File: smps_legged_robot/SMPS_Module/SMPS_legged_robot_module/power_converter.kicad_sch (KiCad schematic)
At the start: 101 parts, among them IC701 LTC3889EUKG#PBF, Q701 IPG20N06S4L26AATMA1, Q702 IPG20N06S4L26AATMA1, Q703 PMBT3906,215, Q704 PMBT3906,215, Q705 IPG20N06S4L26AATMA1, Q706 IPG20N06S4L26AATMA1, Q707 NMOS, Q708 NMOS

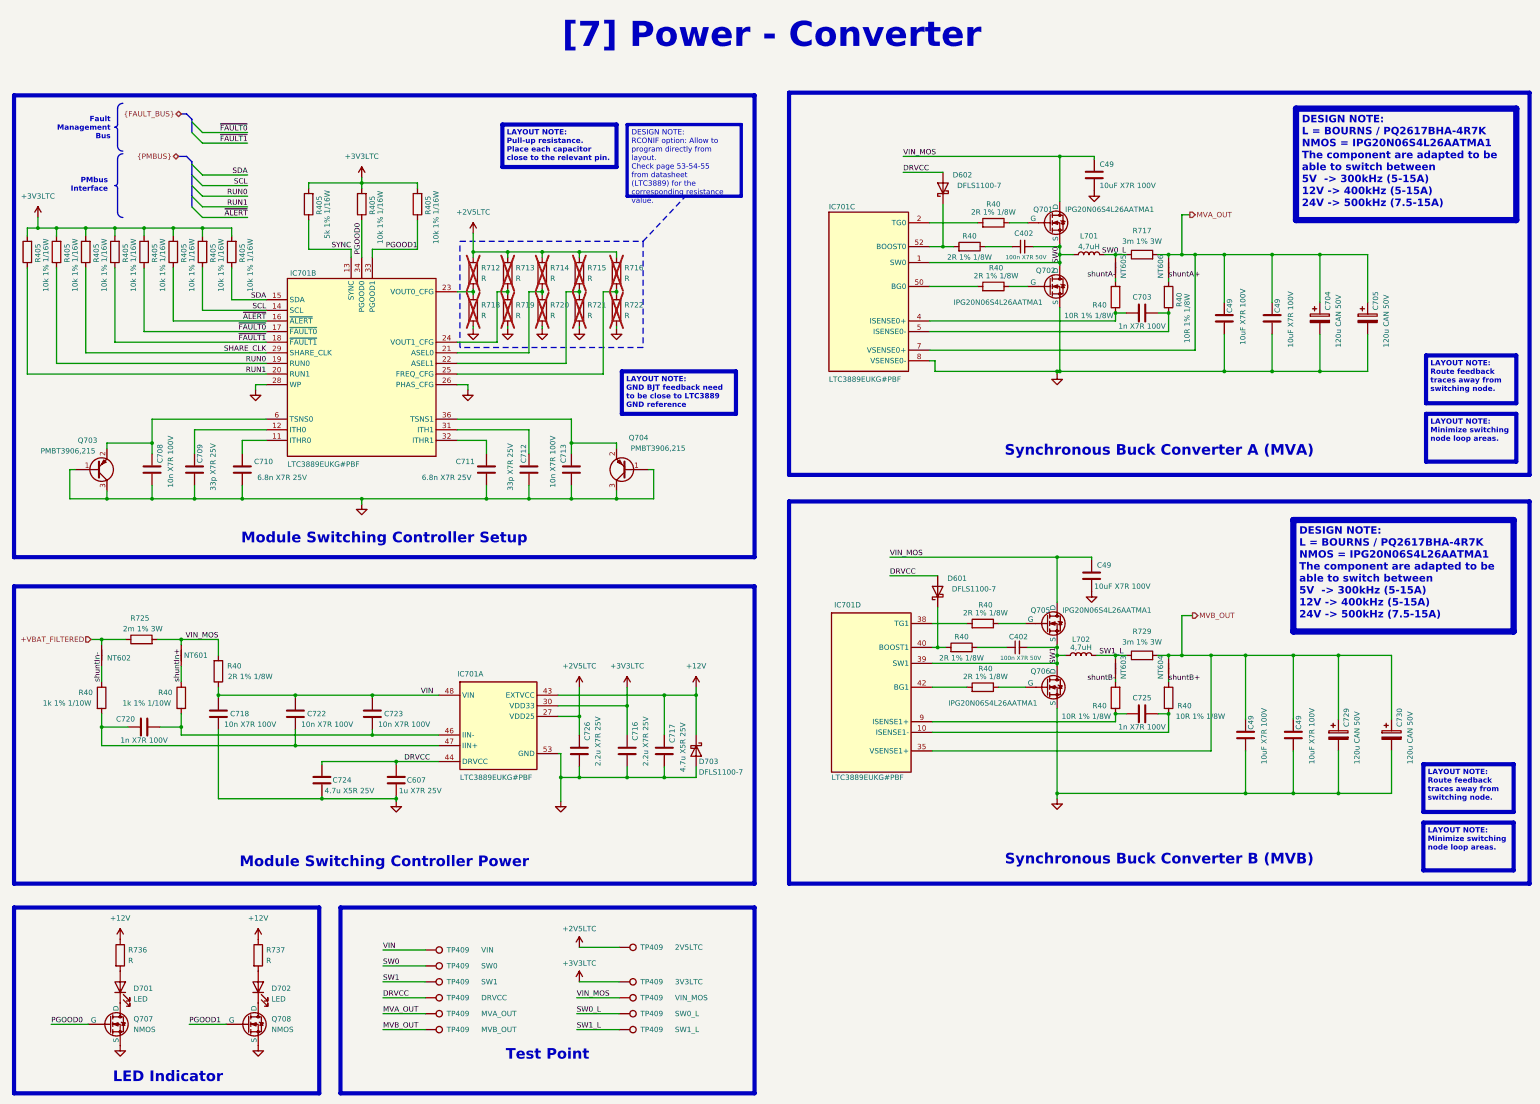
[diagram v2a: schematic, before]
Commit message: Rev 1.0 of smps finished -> waiting for verification
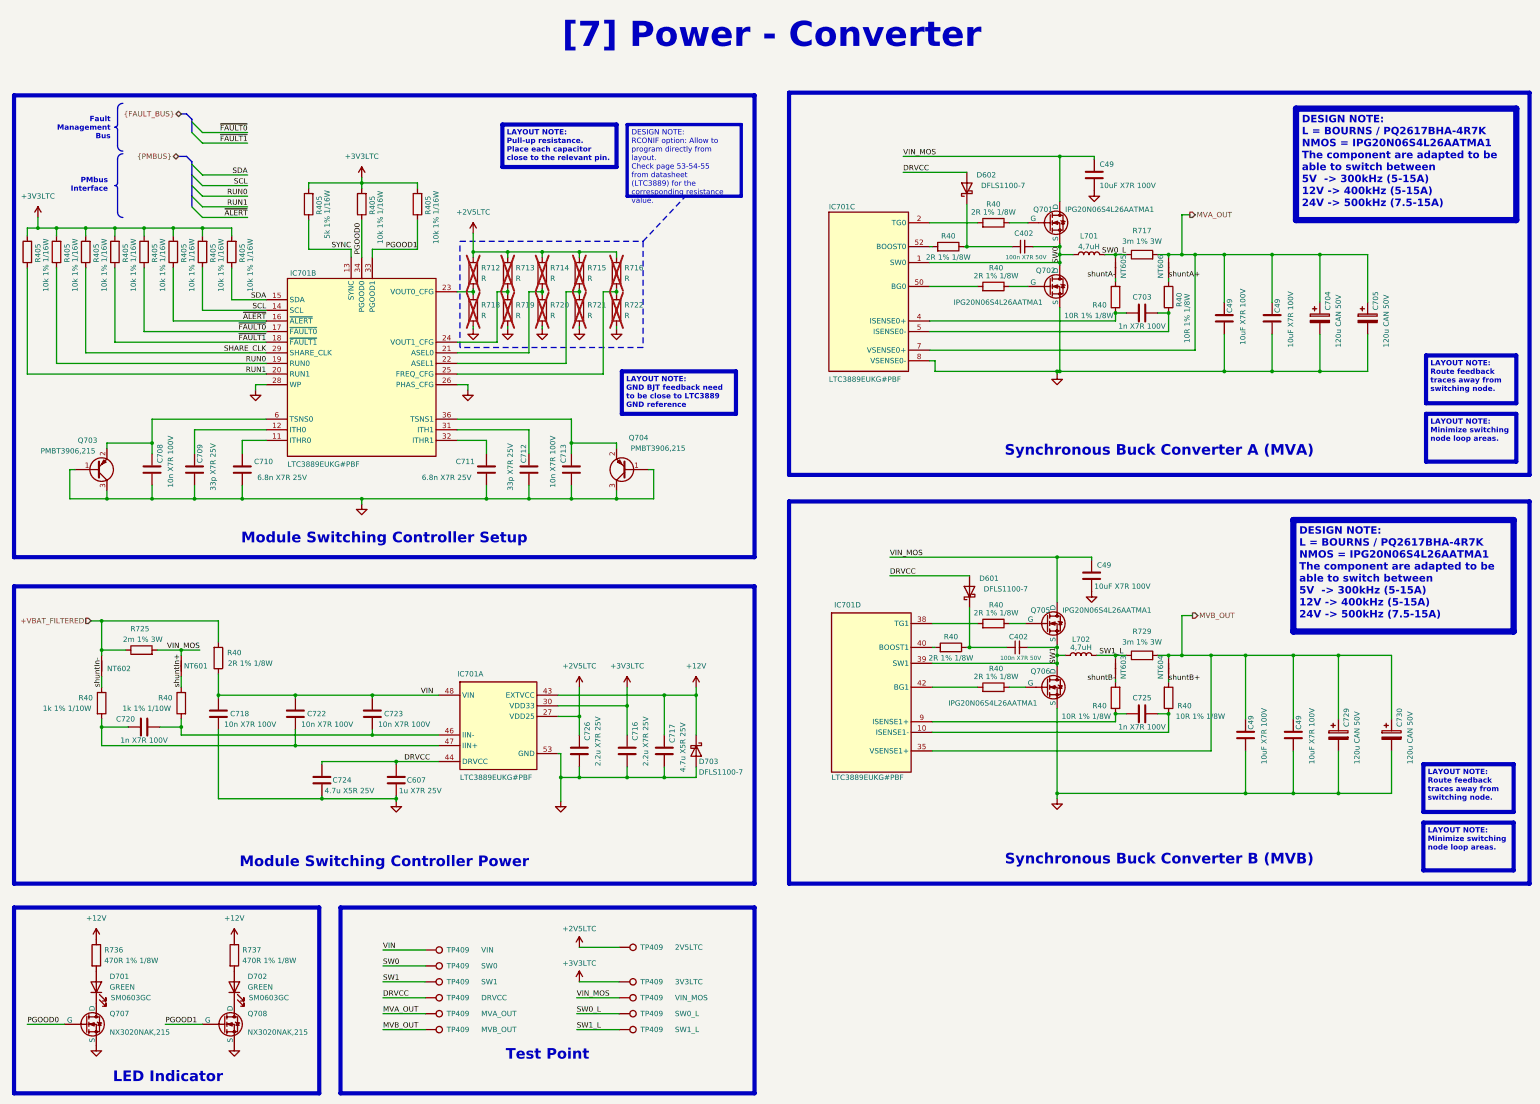
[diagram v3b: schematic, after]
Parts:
- D701, D702: value LED -> GREEN; footprint (none) -> LED_SMD:LED_0603_1608Metric; Digikey ref (none) -> 492-1324-1-ND; Manufacturer ref (none) -> SM0603GC
- Q707, Q708: value NMOS -> NX3020NAK,215; footprint (none) -> 0_package_SOT_TO_SMD:SOT-23-3
- R716, R722: now left out of the parts list
- R736, R737: value R -> 470R 1% 1/8W; footprint (none) -> 0_resistor_smd:R_0402_1005_DensityHigh
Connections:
- net +VBAT_FILTERED: now also R40.2
- net GND: now also Q707.2 (S), Q708.2 (S); no longer Q707.3 (S), Q708.3 (S)
- net PGOOD0: now also Q707.1 (G); no longer Q707.2 (G)
- net PGOOD1: now also Q708.1 (G); no longer Q708.2 (G)
- net VIN_MOS: no longer R40.2
- net at D701.1 (K): now also Q707.3 (D); no longer Q707.1 (D)
- net at C402.1, R40.1: now also D602.1 (K)
- net at IC701.52 (BOOST0), R40.2: no longer D602.1 (K)
- net at C402.1, R40.1: now also D601.1 (K)
- net at IC701.40 (BOOST1), R40.2: no longer D601.1 (K)
- net at D702.1 (K): now also Q708.3 (D); no longer Q708.1 (D)
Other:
- moved on the sheet: D601, D602, NT601, NT602, R40, R725, R736
